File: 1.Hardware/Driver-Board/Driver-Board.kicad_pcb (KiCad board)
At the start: 4 copper layers, 42.3 x 42.3 mm, 75 parts, among them J1 Conn_01x04, J2 Conn_01x02, J3 Conn_01x02, J4 Conn_01x04, J5 Conn_01x02, J6 Conn_01x02, Q1 FDN352AP, SW1 SW_Push, U1 MP2456, U2 MCP1700-3302E_SOT23, U3 TJA1051T-3, U4 AS5600, U5 TB67H450FNG,EL, U6 TB67H450FNG,EL, U7 STM32F103C6Tx, Y1 12MHz

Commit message: updated board
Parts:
- removed D1: B5819W, Diode_SMD:D_SOD-123
- added G***: LOGO, LOGO, F.Cu at (150.0, 100.3)
- L1: value L_Small -> 22uH
- SW1: footprint Button_Switch_SMD:SW_SPST_TL3305B -> custom:KMR731NG LFS
- moved H3 99.4 mm to (165.4, 84.9), turned to -90 degrees
- moved D2 99.2 mm to (168.9, 90.0), turned to 0 degrees
- moved D3 97.9 mm to (168.9, 91.7), turned to 0 degrees
- moved J1 97.0 mm to (160.3, 81.5), turned to -90 degrees
- moved C14 95.6 mm to (165.2, 89.0), turned to 0 degrees
- moved R8 95.6 mm to (166.8, 91.3), turned to -90 degrees
- moved C6 94.3 mm to (160.6, 84.8), turned to -90 degrees
- moved J6 94.0 mm to (170.5, 100.3), turned to 90 degrees
- moved C12 93.6 mm to (165.1, 91.3), turned to -90 degrees
- moved R4 93.1 mm to (159.5, 84.8), turned to 90 degrees
- moved R5 91.9 mm to (158.3, 84.8), turned to 90 degrees
- moved R19 90.9 mm to (165.1, 94.8), turned to -90 degrees
- moved R12 90.8 mm to (157.2, 84.8), turned to -90 degrees
- moved J3 87.9 mm to (166.0, 101.0), turned to 90 degrees
- moved C15 87.2 mm to (163.3, 97.0), turned to 0 degrees
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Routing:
- net GND: track 89.7 -> 72.7 mm, vias 69 -> 67
- net +3.3V: track 60.3 -> 53.9 mm
- net BUCK_SW: track 14.6 -> 9.68 mm
- net CAN-: track 44.6 -> 41.9 mm, vias 2 -> 1
- net CAN+: track 45.0 -> 42.7 mm, vias 2 -> 1
- net BUCK_IN: track 9.83 -> 8.26 mm
- net BUTTON: track 18.8 -> 17.5 mm
- net Net-(U5-RS): track 23.6 -> 24.7 mm
- net Net-(U6-RS): track 19.7 -> 18.7 mm
- net CAN_RX: track 19.5 -> 18.8 mm
- net LED: track 9.84 -> 9.25 mm
- net A_CURRENT: track 6.57 -> 6.05 mm
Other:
- board size 42.3 x 42.3 mm -> 41.2 x 41.3 mm
- board text added: "CLOSED LOOP STEPPER DRIVER TEST BOARD | V1"
- board text added: "H.ELLIS 2024"
- board text removed: "CLOSED LOOP STEPPER MOTOR H-BRIDGE DRIVER TEST BOARD | V1"
- board text removed: "H.ELLIS 2023"
- board text removed: "JLCJLCJLCJLC"

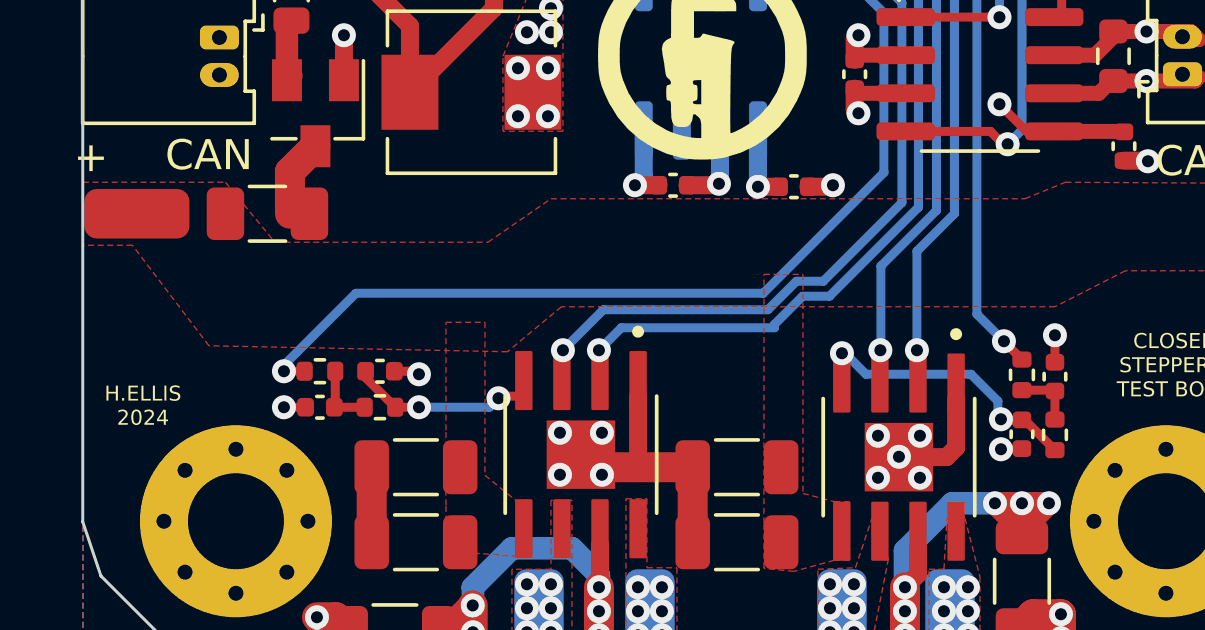
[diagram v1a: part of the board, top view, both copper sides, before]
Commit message: corrected power trace
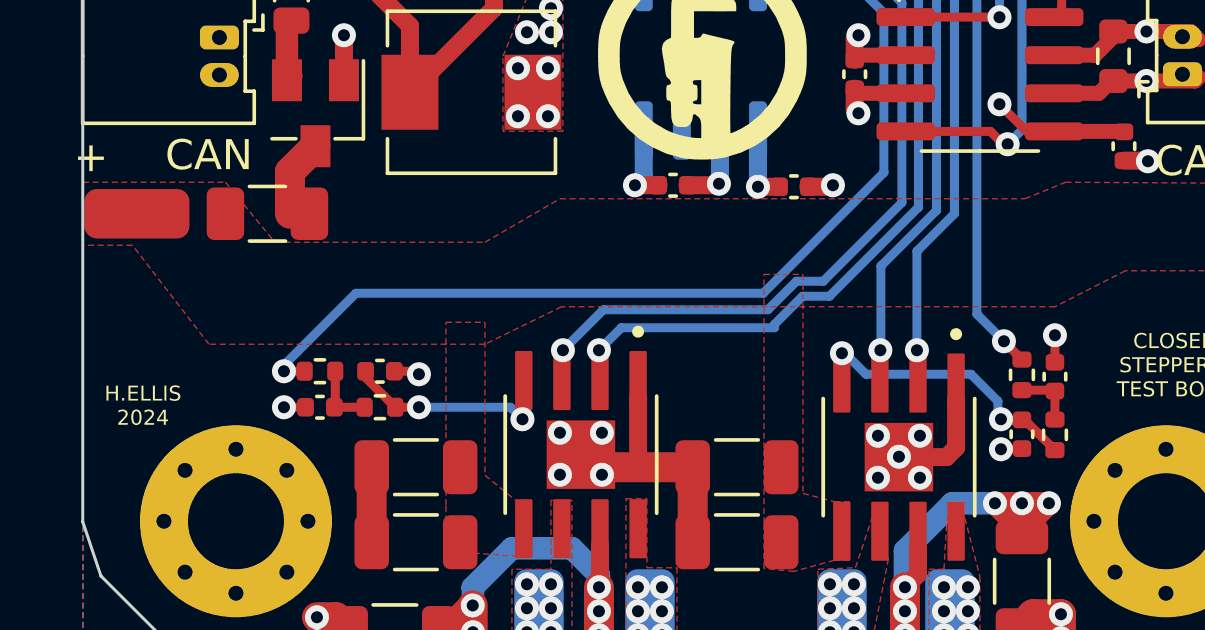
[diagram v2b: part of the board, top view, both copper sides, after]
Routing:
- net A_CURRENT: track 6.05 -> 6.80 mm
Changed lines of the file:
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@@
 		(tags "capacitor")
 		(property "Reference" "C5"
-			(at 0 -1.43 360)
+			(at 0 -1.43 0)
 			(layer "F.Fab")
 			(effects
@@
 		)
 		(property "Value" "10u"
-			(at 0 1.43 360)
+			(at 0 1.43 0)
 			(layer "F.Fab")
 			(effects
@@
 		)
 		(property "Footprint" "Capacitor_SMD:C_0603_1608Metric"
-			(at 0 0 360)
+			(at 0 0 0)
 			(layer "F.Fab")
 			(hide yes)
@@
 		)
 		(property "Datasheet" ""
-			(at 0 0 360)
+			(at 0 0 0)
 			(layer "F.Fab")
 			(hide yes)
@@
 		)
 		(property "Description" ""
-			(at 0 0 360)
+			(at 0 0 0)
 			(layer "F.Fab")
 			(hide yes)
@@
 		)
 		(fp_text user "${REFERENCE}"
-			(at 0 0 360)
+			(at 0 0 0)
 			(layer "F.Fab")
 			(effects
@@
 		)
 		(property "Footprint" "Capacitor_SMD:C_0402_1005Metric"
-			(at 0 0 360)
+			(at 0 0 0)
 			(layer "F.Fab")
 			(hide yes)
@@
 		)
 		(property "Datasheet" ""
-			(at 0 0 360)
+			(at 0 0 0)
 			(layer "F.Fab")
 			(hide yes)
@@
 		)
 		(property "Description" ""
-			(at 0 0 360)
+			(at 0 0 0)
 			(layer "F.Fab")
 			(hide yes)
@@
 		)
 		(property "Footprint" "Capacitor_SMD:C_0402_1005Metric"
-			(at 0 0 360)
+			(at 0 0 0)
 			(layer "F.Fab")
 			(hide yes)
@@
 		)
 		(property "Datasheet" ""
-			(at 0 0 360)
+			(at 0 0 0)
 			(layer "F.Fab")
 			(hide yes)
@@
 		)
 		(property "Description" ""
-			(at 0 0 360)
+			(at 0 0 0)
 			(layer "F.Fab")
 			(hide yes)
@@
 		)
 		(property "Footprint" "Capacitor_SMD:C_0402_1005Metric"
-			(at 0 0 360)
+			(at 0 0 0)
 			(layer "F.Fab")
 			(hide yes)
@@
 		)
 		(property "Datasheet" ""
-			(at 0 0 360)
+			(at 0 0 0)
 			(layer "F.Fab")
 			(hide yes)
@@
 		)
 		(property "Description" ""
-			(at 0 0 360)
+			(at 0 0 0)
 			(layer "F.Fab")
 			(hide yes)
@@
 		(tags "capacitor")
 		(property "Reference" "C4"
-			(at 0 -1.43 360)
+			(at 0 -1.43 0)
 			(layer "F.Fab")
 			(effects
@@
 		)
 		(property "Value" "100n"
-			(at 0 1.43 360)
+			(at 0 1.43 0)
 			(layer "F.Fab")
 			(effects
@@
 		)
 		(property "Footprint" "Capacitor_SMD:C_0603_1608Metric"
-			(at 0 0 360)
+			(at 0 0 0)
 			(layer "F.Fab")
 			(hide yes)
@@
 		)
 		(property "Datasheet" ""
-			(at 0 0 360)
+			(at 0 0 0)
 			(layer "F.Fab")
 			(hide yes)
@@
 		)
 		(property "Description" ""
-			(at 0 0 360)
+			(at 0 0 0)
 			(layer "F.Fab")
 			(hide yes)
@@
 		)
 		(fp_text user "${REFERENCE}"
-			(at 0 0 360)
+			(at 0 0 0)
 			(layer "F.Fab")
 			(effects
@@
 		)
 		(property "Footprint" "Resistor_SMD:R_1206_3216Metric"
-			(at 0 0 360)
+			(at 0 0 0)
 			(layer "F.Fab")
 			(hide yes)
@@
 		)
 		(property "Datasheet" ""
-			(at 0 0 360)
+			(at 0 0 0)
 			(layer "F.Fab")
 			(hide yes)
@@
 		)
 		(property "Description" ""
-			(at 0 0 360)
+			(at 0 0 0)
 			(layer "F.Fab")
 			(hide yes)
@@
 		)
 		(property "Footprint" "Capacitor_SMD:C_1206_3216Metric"
-			(at 0 0 360)
+			(at 0 0 0)
 			(layer "F.Fab")
 			(hide yes)
@@
 		)
 		(property "Datasheet" ""
-			(at 0 0 360)
+			(at 0 0 0)
 			(layer "F.Fab")
 			(hide yes)
@@
 		)
 		(property "Description" ""
-			(at 0 0 360)
+			(at 0 0 0)
 			(layer "F.Fab")
 			(hide yes)
@@
 		)
 		(property "Footprint" "Capacitor_SMD:C_1206_3216Metric"
-			(at 0 0 360)
+			(at 0 0 0)
 			(layer "F.Fab")
 			(hide yes)
@@
 		)
 		(property "Datasheet" ""
-			(at 0 0 360)
+			(at 0 0 0)
 			(layer "F.Fab")
 			(hide yes)
@@
 		)
 		(property "Description" ""
-			(at 0 0 360)
+			(at 0 0 0)
 			(layer "F.Fab")
 			(hide yes)
@@
 		)
 		(property "Footprint" "Capacitor_SMD:C_1206_3216Metric"
-			(at 0 0 360)
+			(at 0 0 0)
 			(layer "F.Fab")
 			(hide yes)
@@
 		)
 		(property "Datasheet" ""
-			(at 0 0 360)
+			(at 0 0 0)
 			(layer "F.Fab")
 			(hide yes)
@@
 		)
 		(property "Description" ""
-			(at 0 0 360)
+			(at 0 0 0)
 			(layer "F.Fab")
 			(hide yes)
@@
 		)
 		(property "Footprint" "Inductor_SMD:L_Sunlord_MWSA0518_5.4x5.2mm"
-			(at 0 0 360)
+			(at 0 0 0)
 			(layer "F.Fab")
 			(hide yes)
@@
 		)
 		(property "Datasheet" ""
-			(at 0 0 360)
+			(at 0 0 0)
 			(layer "F.Fab")
 			(hide yes)
@@
 		)
 		(property "Description" ""
-			(at 0 0 360)
+			(at 0 0 0)
 			(layer "F.Fab")
 			(hide yes)
@@
 		)
 		(property "Footprint" "Crystal:Crystal_SMD_3225-4Pin_3.2x2.5mm"
-			(at 0 0 360)
+			(at 0 0 0)
 			(layer "F.Fab")
 			(hide yes)
@@
 		)
 		(property "Datasheet" ""
-			(at 0 0 360)
+			(at 0 0 0)
 			(layer "F.Fab")
 			(hide yes)
@@
 		)
 		(property "Description" ""
-			(at 0 0 360)
+			(at 0 0 0)
 			(layer "F.Fab")
 			(hide yes)
@@
 		)
 		(property "Footprint" "Resistor_SMD:R_0402_1005Metric"
-			(at 0 0 360)
+			(at 0 0 0)
 			(layer "F.Fab")
 			(hide yes)
@@
 		)
 		(property "Datasheet" ""
-			(at 0 0 360)
+			(at 0 0 0)
 			(layer "F.Fab")
 			(hide yes)
@@
 		)
 		(property "Description" ""
-			(at 0 0 360)
+			(at 0 0 0)
 			(layer "F.Fab")
 			(hide yes)
@@
 		)
 		(property "Footprint" "Capacitor_SMD:C_1206_3216Metric"
-			(at 0 0 360)
+			(at 0 0 0)
 			(layer "F.Fab")
 			(hide yes)
@@
 		)
 		(property "Datasheet" ""
-			(at 0 0 360)
+			(at 0 0 0)
 			(layer "F.Fab")
 			(hide yes)
@@
 		)
 		(property "Description" ""
-			(at 0 0 360)
+			(at 0 0 0)
 			(layer "F.Fab")
 			(hide yes)
@@
 		)
 		(property "Footprint" "Capacitor_SMD:C_0402_1005Metric"
-			(at 0 0 360)
+			(at 0 0 0)
 			(layer "F.Fab")
 			(hide yes)
@@
 		)
 		(property "Datasheet" ""
-			(at 0 0 360)
+			(at 0 0 0)
 			(layer "F.Fab")
 			(hide yes)
@@
 		)
 		(property "Description" ""
-			(at 0 0 360)
+			(at 0 0 0)
 			(layer "F.Fab")
 			(hide yes)
@@
 		)
 		(property "Footprint" "StepperConnections:Stepper Wire Connector"
-			(at 0 0 360)
+			(at 0 0 0)
 			(layer "F.Fab")
 			(hide yes)
@@
 		)
 		(property "Datasheet" ""
-			(at 0 0 360)
+			(at 0 0 0)
 			(layer "F.Fab")
 			(hide yes)
@@
 		)
 		(property "Description" ""
-			(at 0 0 360)
+			(at 0 0 0)
 			(layer "F.Fab")
 			(hide yes)
@@
 	)
 	(segment
-		(start 143.2 111.8)
-		(end 143.27 111.73)
+		(start 138.77 111.11)
+		(end 139.76 112.1)
 		(width 0.3)
 		(layer "F.Cu")
@@
 	)
 	(segment
-		(start 138.77 111.11)
-		(end 139.76 112.1)
+		(start 138.77 110.9)
+		(end 138.77 111.11)
 		(width 0.3)
 		(layer "F.Cu")
@@
 	)
 	(segment
-		(start 138.77 110.9)
-		(end 138.77 111.11)
+		(start 144 112.5)
+		(end 144 111.775)
 		(width 0.3)
 		(layer "F.Cu")
@@
 	)
 	(segment
-		(start 143.27 111.73)
+		(start 144 111.775)
 		(end 144.045 111.73)
 		(width 0.3)
@@
 	)
 	(via
-		(at 143.2 111.8)
+		(at 144 112.5)
 		(size 0.8)
 		(drill 0.4)
@@
 	)
 	(segment
-		(start 143.2 111.8)
-		(end 142.9 112.1)
+		(start 144 112.5)
+		(end 143.6 112.1)
 		(width 0.3)
 		(layer "B.Cu")
@@
 	)
 	(segment
-		(start 142.9 112.1)
+		(start 143.6 112.1)
 		(end 140.55 112.1)
 		(width 0.3)
@@
 		(polygon
 			(pts
-				(xy 168.65 107.55) (xy 164.1 107.55) (xy 161.75 108.75) (xy 145.3 108.75) (xy 143.5 110.25) (xy 133.55 110.05)
-				(xy 131 106.7) (xy 129.35 106.7) (xy 129.35 104.6) (xy 134.1 104.6) (xy 135.75 106.6) (xy 142.85 106.6)
-				(xy 144.95 105.15) (xy 160.75 105.15) (xy 162.1 104.6) (xy 170.55 104.65) (xy 170.55 106.05)
+				(xy 168.65 107.55) (xy 164.1 107.55) (xy 161.75 108.75) (xy 145.3 108.75) (xy 142.75 110) (xy 133.55 110)
+				(xy 131 106.7) (xy 129.35 106.7) (xy 129.35 104.6) (xy 134.1 104.6) (xy 135.75 106.6) (xy 142.75 106.6)
+				(xy 145.25 105.15) (xy 160.75 105.15) (xy 162.1 104.6) (xy 170.55 104.65) (xy 170.55 106.05)
 			)
 		)

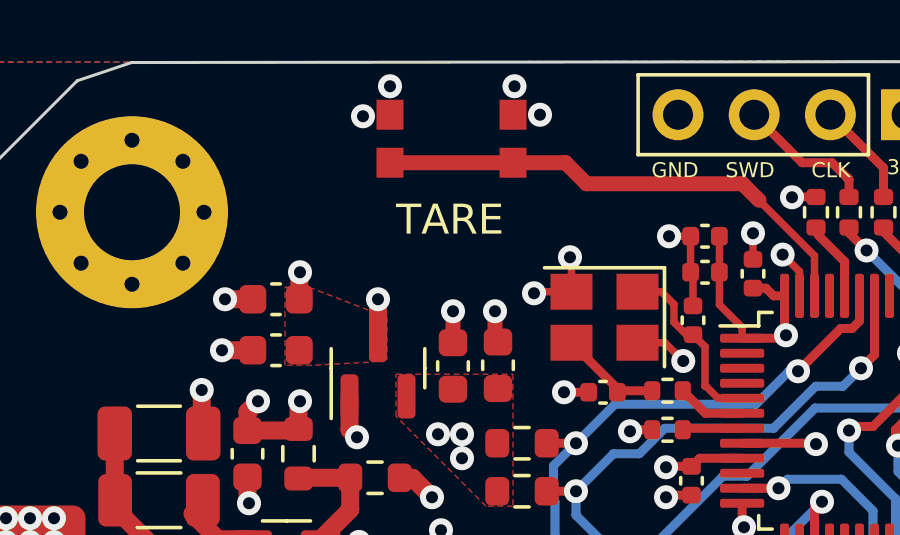
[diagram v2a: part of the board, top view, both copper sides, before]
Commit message: libopencm3 integration and power test
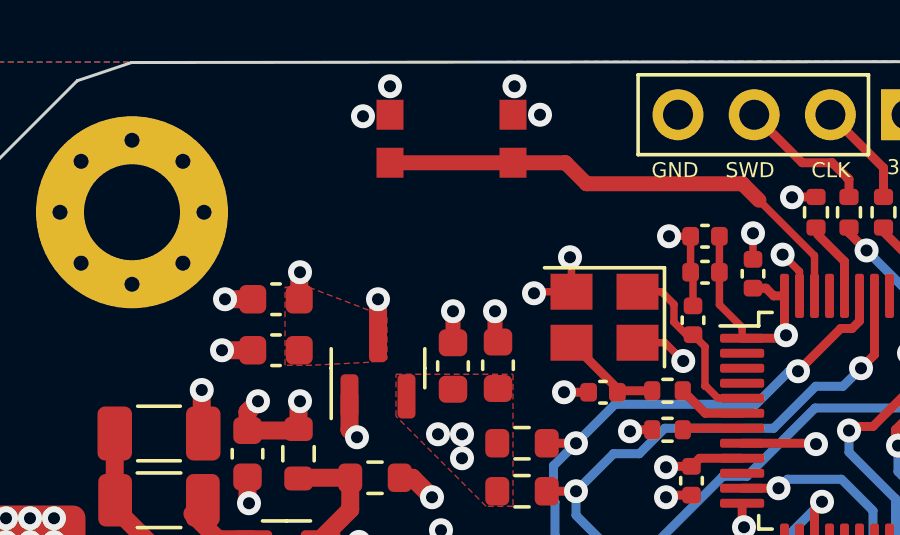
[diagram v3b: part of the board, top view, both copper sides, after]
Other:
- board text removed: "TARE"
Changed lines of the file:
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@@
-		)
-	)
-	(gr_text "TARE"
-		(at 145.05 85.05 0)
-		(layer "F.SilkS")
-		(effects
-			(font
-				(size 1 1)
-				(thickness 0.15)
-			)
 		)
 	)
